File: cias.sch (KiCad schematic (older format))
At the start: 63 parts, among them CN13 KEYBOARD, CN6 SERIAL_DB25M, CN7 PARALLEL_DB25F, Q501 2N3904, Q502 2N3906, Q503 2N3906, Q711 2N3904, U38 MC1488, U39 MC1489, U42 NE555, U7 VIA_8520, U8 VIA_8520

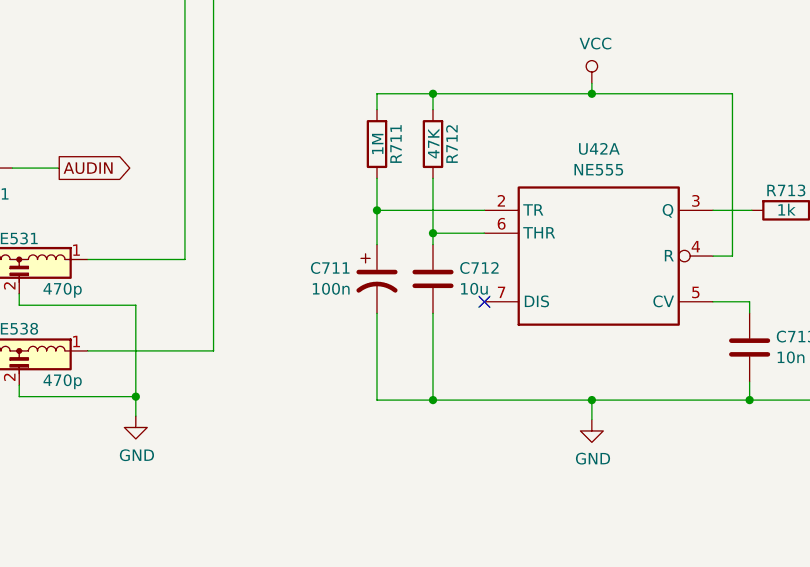
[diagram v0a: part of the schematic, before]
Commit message: Fix wrong symbols in schematics - Does not impact PCB
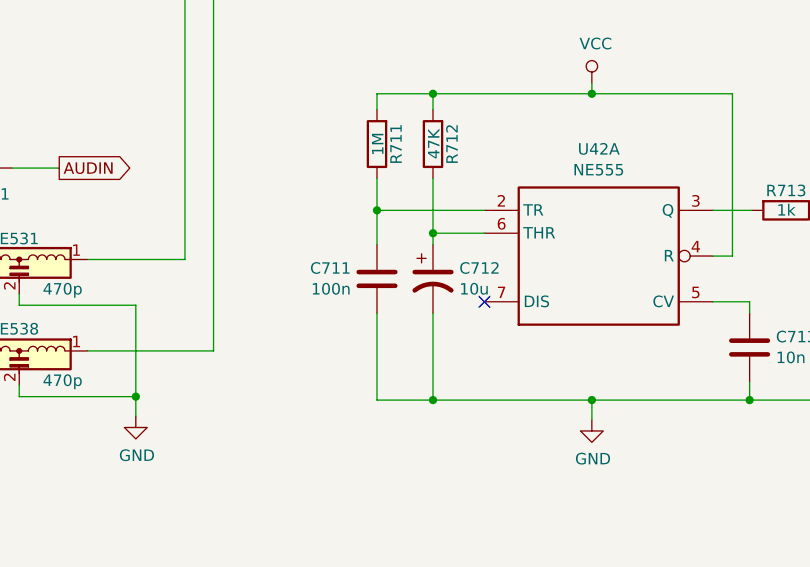
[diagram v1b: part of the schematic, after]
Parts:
- removed C711: 100n, Raemixx500:C_Axial_L9.0mm_D3.2mm_P12.70mm, symbol Device:CP1
- removed C712: 10u, Capacitor_THT:CP_Radial_D8.0mm_P5.00mm, symbol Device:C
- added C711: 100n, Raemixx500:C_Axial_L9.0mm_D3.2mm_P12.70mm, symbol Device:C
- added C712: 10u, Capacitor_THT:CP_Radial_D8.0mm_P5.00mm, symbol Device:CP1
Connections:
- net GND: now also C711.2, C712.2
- net at R711.1, U42.2 (TR): now also C711.1
- net at R712.1, U42.6 (THR): now also C712.1
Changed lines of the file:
@@
 Connection ~ 11990 7595
 NoConn ~ 12215 7895
-$Comp
-L Device:CP1 C711
-U 1 1 60129516
-P 11745 7795
-F 0 "C711" H 11631 7841 50  0000 R CNN
-F 1 "100n" H 11631 7750 50  0000 R CNN
-F 2 "Raemixx500:C_Axial_L9.0mm_D3.2mm_P12.70mm" H 11745 7795 50  0001 C CNN
-F 3 "~" H 11745 7795 50  0001 C CNN
-	1    11745 7795
-	1    0    0    -1
-$EndComp
-$Comp
-L Device:C C712
-U 1 1 60174D47
-P 11990 7795
-F 0 "C712" H 12105 7841 50  0000 L CNN
-F 1 "10u" H 12105 7750 50  0000 L CNN
-F 2 "Capacitor_THT:CP_Radial_D8.0mm_P5.00mm" H 12028 7645 50  0001 C CNN
-F 3 "~" H 11990 7795 50  0001 C CNN
-	1    11990 7795
-	1    0    0    -1
-$EndComp
 Wire Wire Line
 	11745 7645 11745 7495
@@
 	0    -1   -1   0
 $EndComp
+$Comp
+L Device:CP1 C712
+U 1 1 5EBE40E3
+P 11990 7795
+F 0 "C712" H 12105 7841 50  0000 L CNN
+F 1 "10u" H 12105 7750 50  0000 L CNN
+F 2 "Capacitor_THT:CP_Radial_D8.0mm_P5.00mm" H 11990 7795 50  0001 C CNN
+F 3 "~" H 11990 7795 50  0001 C CNN
+	1    11990 7795
+	1    0    0    -1
+$EndComp
+$Comp
+L Device:C C711
+U 1 1 5EBE45B6
+P 11745 7795
+F 0 "C711" H 11631 7841 50  0000 R CNN
+F 1 "100n" H 11631 7750 50  0000 R CNN
+F 2 "Raemixx500:C_Axial_L9.0mm_D3.2mm_P12.70mm" H 11783 7645 50  0001 C CNN
+F 3 "~" H 11745 7795 50  0001 C CNN
+	1    11745 7795
+	1    0    0    -1
+$EndComp
 Wire Bus Line

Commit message: Begin adding part numbers
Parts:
- C39, C7, C8: Cost (none) -> 0.071; MFG Name (none) -> KEMET; MFG Part Num (none) -> C410C103K1H5TAAUTO
- C42: Cost (none) -> 0.078; MFG Name (none) -> KEMET; MFG Part Num (none) -> C412C334M5U5TA; Optional (none) -> POR
- C501, C502: Cost (none) -> 0.078; MFG Name (none) -> KEMET; MFG Part Num (none) -> C412C334M5U5TA
- C711: Cost (none) -> 0.035; MFG Name (none) -> AVX; MFG Part Num (none) -> SA115C104KAR; Optional (none) -> POR
- C712, Q711, R711, R712, R713, U42: Optional (none) -> POR
- C713: Cost (none) -> 0.071; MFG Name (none) -> KEMET; MFG Part Num (none) -> C410C103K1H5TAAUTO; Optional (none) -> POR
- CN13: Optional (none) -> KEYBOARD
- CN6, U38, U39: Optional (none) -> SERIAL
- CN7: Optional (none) -> PARALLEL
- JP1, JP7B1: MFG Name (none) -> SKIP; MFG Part Num (none) -> SKIP; Optional (none) -> JMP
- R503, R504: Optional (none) -> ROM
- U7, U8: Optional (none) -> CUSTOM
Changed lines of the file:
@@
 F 2 "Package_DIP:DIP-40_W15.24mm_Socket_LongPads" H 3315 3460 50  0001 C CNN
 F 3 "DOCUMENTATION" H 3315 3460 50  0001 C CNN
+F 4 "CUSTOM" H 3315 3460 50  0001 C CNN "Optional"
 	1    3315 3460
 	1    0    0    -1
@@
 F 2 "Package_DIP:DIP-40_W15.24mm_Socket_LongPads" H 3315 6325 50  0001 C CNN
 F 3 "DOCUMENTATION" H 3315 6325 50  0001 C CNN
+F 4 "CUSTOM" H 3315 6325 50  0001 C CNN "Optional"
 	1    3315 6325
 	1    0    0    -1
@@
 F 2 "Raemixx500:DB_25F" H 9255 2590 50  0001 C CNN
 F 3 " ~" H 9255 2590 50  0001 C CNN
+F 4 "PARALLEL" H 9255 2590 50  0001 C CNN "Optional"
 	1    9255 2590
 	1    0    0    -1
@@
 F 2 "Raemixx500:DB_25M" H 9255 7610 50  0001 C CNN
 F 3 " ~" H 9255 7610 50  0001 C CNN
+F 4 "SERIAL" H 9255 7610 50  0001 C CNN "Optional"
 	1    9255 7610
 	1    0    0    1
@@
 F 2 "Raemixx500:C_Axial_L9.0mm_D3.2mm_P12.70mm" H 10050 7310 50  0001 C CNN
 F 3 "~" H 10050 7310 50  0001 C CNN
+F 4 "KEMET" H 10050 7310 50  0001 C CNN "MFG Name"
+F 5 "C412C334M5U5TA" H 10050 7310 50  0001 C CNN "MFG Part Num"
+F 6 "0.078" H 10050 7310 50  0001 C CNN "Cost"
 	1    10050 7310
 	0    1    1    0
@@
 F 2 "Raemixx500:C_Axial_L9.0mm_D3.2mm_P12.70mm" H 7935 8610 50  0001 C CNN
 F 3 "~" H 7935 8610 50  0001 C CNN
+F 4 "KEMET" H 7935 8610 50  0001 C CNN "MFG Name"
+F 5 "C412C334M5U5TA" H 7935 8610 50  0001 C CNN "MFG Part Num"
+F 6 "0.078" H 7935 8610 50  0001 C CNN "Cost"
 	1    7935 8610
 	0    1    1    0
@@
 F 2 "Package_DIP:DIP-14_W7.62mm_Socket_LongPads" H 7250 6360 50  0001 C CNN
 F 3 "DOCUMENTATION" H 7250 6260 50  0001 C CNN
+F 4 "SERIAL" H 7250 6610 50  0001 C CNN "Optional"
 	3    7250 6610
 	1    0    0    -1
@@
 F 2 "Package_DIP:DIP-14_W7.62mm_Socket_LongPads" H 7250 5945 50  0001 C CNN
 F 3 "DOCUMENTATION" H 7250 5845 50  0001 C CNN
+F 4 "SERIAL" H 7250 6195 50  0001 C CNN "Optional"
 	4    7250 6195
 	1    0    0    -1
@@
 F 2 "Package_DIP:DIP-14_W7.62mm_Socket_LongPads" H 7250 6760 50  0001 C CNN
 F 3 "DOCUMENTATION" H 7250 6660 50  0001 C CNN
+F 4 "SERIAL" H 7250 7010 50  0001 C CNN "Optional"
 	2    7250 7010
 	1    0    0    -1
@@
 F 2 "Package_DIP:DIP-14_W7.62mm_Socket_LongPads" H 6445 6560 50  0001 C CNN
 F 3 "DOCUMENTATION" H 6445 6460 50  0001 C CNN
+F 4 "SERIAL" H 6445 6810 50  0001 C CNN "Optional"
 	1    6445 6810
 	-1   0    0    -1
@@
 F 2 "Package_DIP:DIP-14_W7.62mm_Socket_LongPads" H 6090 7160 50  0001 C CNN
 F 3 "DOCUMENTATION" H 6090 7060 50  0001 C CNN
+F 4 "SERIAL" H 6090 7410 50  0001 C CNN "Optional"
 	2    6090 7410
 	-1   0    0    -1
@@
 F 2 "Package_DIP:DIP-14_W7.62mm_Socket_LongPads" H 5585 7560 50  0001 C CNN
 F 3 "DOCUMENTATION" H 5585 7460 50  0001 C CNN
+F 4 "SERIAL" H 5585 7810 50  0001 C CNN "Optional"
 	3    5585 7810
 	-1   0    0    -1
@@
 F 2 "Package_DIP:DIP-14_W7.62mm_Socket_LongPads" H 5585 6960 50  0001 C CNN
 F 3 "DOCUMENTATION" H 5585 6860 50  0001 C CNN
+F 4 "SERIAL" H 5585 7210 50  0001 C CNN "Optional"
 	4    5585 7210
 	-1   0    0    -1
@@
 F 2 "Package_DIP:DIP-14_W7.62mm_Socket_LongPads" H 1525 10110 50  0001 C CNN
 F 3 "DOCUMENTATION" H 1525 10010 50  0001 C CNN
+F 4 "SERIAL" H 1525 10360 50  0001 C CNN "Optional"
 	5    1525 10360
 	1    0    0    -1
@@
 F 2 "Package_DIP:DIP-14_W7.62mm_Socket_LongPads" H 2165 10110 50  0001 C CNN
 F 3 "DOCUMENTATION" H 2165 10010 50  0001 C CNN
+F 4 "SERIAL" H 2165 10360 50  0001 C CNN "Optional"
 	5    2165 10360
 	1    0    0    -1
@@
 F 2 "Raemixx500:C_Axial_L9.0mm_D3.2mm_P12.70mm" H 1228 10210 50  0001 C CNN
 F 3 "~" H 1190 10360 50  0001 C CNN
+F 4 "KEMET" H 1190 10360 50  0001 C CNN "MFG Name"
+F 5 "C410C103K1H5TAAUTO" H 1190 10360 50  0001 C CNN "MFG Part Num"
+F 6 "0.071" H 1190 10360 50  0001 C CNN "Cost"
 	1    1190 10360
 	1    0    0    -1
@@
 F 2 "Raemixx500:R_Axial_DIN0309_L9.0mm_D3.2mm_P12.70mm_Horizontal" V 12745 2745 50  0001 C CNN
 F 3 "~" H 12815 2745 50  0001 C CNN
+F 4 "ROM" H 12815 2745 50  0001 C CNN "Optional"
 	1    12815 2745
 	0    1    1    0
@@
 F 2 "Raemixx500:Keyboard_Connector" H 15110 3390 50  0001 C CNN
 F 3 "" H 15110 3390 50  0001 C CNN
+F 4 "KEYBOARD" H 15110 3390 50  0001 C CNN "Optional"
 	1    15110 3390
 	1    0    0    1
@@
 F 2 "Raemixx500:R_Axial_DIN0309_L9.0mm_D3.2mm_P12.70mm_Horizontal" V 12745 3675 50  0001 C CNN
 F 3 "~" H 12815 3675 50  0001 C CNN
+F 4 "ROM" H 12815 3675 50  0001 C CNN "Optional"
 	1    12815 3675
 	0    1    1    0
@@
 F 2 "Package_DIP:DIP-8_W7.62mm_Socket_LongPads" H 12715 7695 50  0001 C CNN
 F 3 "http://www.ti.com/lit/ds/symlink/ne555.pdf" H 12715 7695 50  0001 C CNN
+F 4 "POR" H 12715 7695 50  0001 C CNN "Optional"
 	1    12715 7695
 	1    0    0    -1
@@
 F 2 "Raemixx500:R_Axial_DIN0309_L9.0mm_D3.2mm_P12.70mm_Horizontal" V 11920 7205 50  0001 C CNN
 F 3 "~" H 11990 7205 50  0001 C CNN
+F 4 "POR" H 11990 7205 50  0001 C CNN "Optional"
 	1    11990 7205
 	-1   0    0    1
@@
 F 2 "Raemixx500:R_Axial_DIN0309_L9.0mm_D3.2mm_P12.70mm_Horizontal" V 11675 7205 50  0001 C CNN
 F 3 "~" H 11745 7205 50  0001 C CNN
+F 4 "POR" H 11745 7205 50  0001 C CNN "Optional"
 	1    11745 7205
 	-1   0    0    1
@@
 F 2 "Raemixx500:C_Axial_L9.0mm_D3.2mm_P12.70mm" H 13413 7945 50  0001 C CNN
 F 3 "~" H 13375 8095 50  0001 C CNN
+F 4 "KEMET" H 13375 8095 50  0001 C CNN "MFG Name"
+F 5 "C410C103K1H5TAAUTO" H 13375 8095 50  0001 C CNN "MFG Part Num"
+F 6 "0.071" H 13375 8095 50  0001 C CNN "Cost"
+F 7 "POR" H 13375 8095 50  0001 C CNN "Optional"
 	1    13375 8095
 	1    0    0    -1
@@
 F 2 "Package_TO_SOT_THT:TO-92L_Inline_Wide" H 14115 7420 50  0001 L CIN
 F 3 "https://www.fairchildsemi.com/datasheets/2N/2N3904.pdf" H 13915 7495 50  0001 L CNN
+F 4 "POR" H 13915 7495 50  0001 C CNN "Optional"
 	1    13915 7495
 	1    0    0    -1
@@
 F 2 "Raemixx500:Jumper2-Bridged" H 14310 7160 50  0001 C CNN
 F 3 "~" H 14310 7160 50  0001 C CNN
+F 4 "SKIP" H 14310 7160 50  0001 C CNN "MFG Name"
+F 5 "SKIP" H 14310 7160 50  0001 C CNN "MFG Part Num"
+F 6 "JMP" H 14310 7160 50  0001 C CNN "Optional"
 	1    14310 7160
 	1    0    0    -1
@@
 F 2 "Package_DIP:DIP-8_W7.62mm_Socket_LongPads" H 15630 7720 50  0001 C CNN
 F 3 "http://www.ti.com/lit/ds/symlink/lm555.pdf" H 15630 7720 50  0001 C CNN
+F 4 "POR" H 15630 7720 50  0001 C CNN "Optional"
 	2    15630 7720
 	1    0    0    -1
@@
 F 2 "Raemixx500:C_Axial_L6.3mm_D2.5mm_P10.16mm" H 15333 7635 50  0001 C CNN
 F 3 "~" H 15295 7785 50  0001 C CNN
+F 4 "KEMET" H 15295 7785 50  0001 C CNN "MFG Name"
+F 5 "C412C334M5U5TA" H 15295 7785 50  0001 C CNN "MFG Part Num"
+F 6 "0.078" H 15295 7785 50  0001 C CNN "Cost"
+F 7 "POR" H 15295 7785 50  0001 C CNN "Optional"
 	1    15295 7785
 	1    0    0    -1
@@
 F 2 "Package_DIP:DIP-40_W15.24mm_Socket_LongPads" H 6260 10260 50  0001 C CNN
 F 3 "DOCUMENTATION" H 6260 10260 50  0001 C CNN
+F 4 "CUSTOM" H 6260 10260 50  0001 C CNN "Optional"
 	2    6260 10260
 	1    0    0    -1
@@
 F 2 "Package_DIP:DIP-40_W15.24mm_Socket_LongPads" H 7675 10260 50  0001 C CNN
 F 3 "DOCUMENTATION" H 7675 10260 50  0001 C CNN
+F 4 "CUSTOM" H 7675 10260 50  0001 C CNN "Optional"
 	2    7675 10260
 	1    0    0    -1
@@
 F 2 "Raemixx500:C_Axial_L6.3mm_D2.5mm_P10.16mm" H 7043 10090 50  0001 C CNN
 F 3 "~" H 7005 10240 50  0001 C CNN
+F 4 "KEMET" H 7005 10240 50  0001 C CNN "MFG Name"
+F 5 "C410C103K1H5TAAUTO" H 7005 10240 50  0001 C CNN "MFG Part Num"
+F 6 "0.071" H 7005 10240 50  0001 C CNN "Cost"
 	1    7005 10240
 	1    0    0    -1
@@
 F 2 "Raemixx500:C_Axial_L6.3mm_D2.5mm_P10.16mm" H 8493 10090 50  0001 C CNN
 F 3 "~" H 8455 10240 50  0001 C CNN
+F 4 "KEMET" H 8455 10240 50  0001 C CNN "MFG Name"
+F 5 "C410C103K1H5TAAUTO" H 8455 10240 50  0001 C CNN "MFG Part Num"
+F 6 "0.071" H 8455 10240 50  0001 C CNN "Cost"
 	1    8455 10240
 	1    0    0    -1
@@
 F 2 "Raemixx500:R_Axial_DIN0309_L9.0mm_D3.2mm_P12.70mm_Horizontal" V 13465 7495 50  0001 C CNN
 F 3 "~" H 13535 7495 50  0001 C CNN
+F 4 "POR" H 13535 7495 50  0001 C CNN "Optional"
 	1    13535 7495
 	0    1    1    0
@@
 F 2 "Raemixx500:Jumper3-Bridged23" H 1240 4360 50  0001 C CNN
 F 3 "~" H 1240 4360 50  0001 C CNN
+F 4 "SKIP" H 1240 4360 50  0001 C CNN "MFG Name"
+F 5 "SKIP" H 1240 4360 50  0001 C CNN "MFG Part Num"
+F 6 "JMP" H 1240 4360 50  0001 C CNN "Optional"
 	1    1240 4360
 	0    -1   -1   0
@@
 F 2 "Capacitor_THT:CP_Radial_D8.0mm_P5.00mm" H 11990 7795 50  0001 C CNN
 F 3 "~" H 11990 7795 50  0001 C CNN
+F 4 "POR" H 11990 7795 50  0001 C CNN "Optional"
 	1    11990 7795
 	1    0    0    -1
@@
 F 2 "Raemixx500:C_Axial_L9.0mm_D3.2mm_P12.70mm" H 11783 7645 50  0001 C CNN
 F 3 "~" H 11745 7795 50  0001 C CNN
+F 4 "0.035" H 11745 7795 50  0001 C CNN "Cost"
+F 5 "AVX" H 11745 7795 50  0001 C CNN "MFG Name"
+F 6 "SA115C104KAR" H 11745 7795 50  0001 C CNN "MFG Part Num"
+F 7 "POR" H 11745 7795 50  0001 C CNN "Optional"
 	1    11745 7795
 	1    0    0    -1

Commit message: More part numbers
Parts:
- C501, C502, D501, E502, E503, E531, E532, E533, E534, E535, E536, E537, E538, Q501, R501, R502: Optional (none) -> SERIAL
- E501, E511, E512, E513, E514, E515, E516, E517, E518, E519, E520, E521, E522, E523, E524: Optional (none) -> PARALLEL
- E631, E632, Q502, Q503, R505, R506, R507: Optional (none) -> KEYBOARD
- R109: Optional (none) -> PARALLEL/SERIAL/FLOPPY
- R503, R504: Optional ROM -> KEYBOARD
- RP501: Optional (none) -> KEYBOARD/FLOPPY/PARALLEL/MEMORY

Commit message: More part numbers
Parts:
- C712: Cost (none) -> 0.196; MFG Name (none) -> PANASONIC; MFG Part Num (none) -> EEUFR1H100
- U38: Cost (none) -> 0.615; MFG Name (none) -> TI; MFG Part Num (none) -> MC1488N
- U39: Cost (none) -> 0.668; MFG Name (none) -> TI; MFG Part Num (none) -> MC1489N
- U42: Cost (none) -> 0.315; MFG Name (none) -> TI; MFG Part Num (none) -> NE555P
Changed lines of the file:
@@
 F 3 "DOCUMENTATION" H 7250 6260 50  0001 C CNN
 F 4 "SERIAL" H 7250 6610 50  0001 C CNN "Optional"
+F 5 "0.615" H 7250 6610 50  0001 C CNN "Cost"
+F 6 "TI" H 7250 6610 50  0001 C CNN "MFG Name"
+F 7 "MC1488N" H 7250 6610 50  0001 C CNN "MFG Part Num"
 	3    7250 6610
 	1    0    0    -1
@@
 F 3 "DOCUMENTATION" H 7250 5845 50  0001 C CNN
 F 4 "SERIAL" H 7250 6195 50  0001 C CNN "Optional"
+F 5 "0.615" H 7250 6195 50  0001 C CNN "Cost"
+F 6 "TI" H 7250 6195 50  0001 C CNN "MFG Name"
+F 7 "MC1488N" H 7250 6195 50  0001 C CNN "MFG Part Num"
 	4    7250 6195
 	1    0    0    -1
@@
 F 3 "DOCUMENTATION" H 7250 6660 50  0001 C CNN
 F 4 "SERIAL" H 7250 7010 50  0001 C CNN "Optional"
+F 5 "0.615" H 7250 7010 50  0001 C CNN "Cost"
+F 6 "TI" H 7250 7010 50  0001 C CNN "MFG Name"
+F 7 "MC1488N" H 7250 7010 50  0001 C CNN "MFG Part Num"
 	2    7250 7010
 	1    0    0    -1
@@
 F 3 "DOCUMENTATION" H 6445 6460 50  0001 C CNN
 F 4 "SERIAL" H 6445 6810 50  0001 C CNN "Optional"
+F 5 "0.668" H 6445 6810 50  0001 C CNN "Cost"
+F 6 "TI" H 6445 6810 50  0001 C CNN "MFG Name"
+F 7 "MC1489N" H 6445 6810 50  0001 C CNN "MFG Part Num"
 	1    6445 6810
 	-1   0    0    -1
@@
 F 3 "DOCUMENTATION" H 6090 7060 50  0001 C CNN
 F 4 "SERIAL" H 6090 7410 50  0001 C CNN "Optional"
+F 5 "0.668" H 6090 7410 50  0001 C CNN "Cost"
+F 6 "TI" H 6090 7410 50  0001 C CNN "MFG Name"
+F 7 "MC1489N" H 6090 7410 50  0001 C CNN "MFG Part Num"
 	2    6090 7410
 	-1   0    0    -1
@@
 F 3 "DOCUMENTATION" H 5585 7460 50  0001 C CNN
 F 4 "SERIAL" H 5585 7810 50  0001 C CNN "Optional"
+F 5 "0.668" H 5585 7810 50  0001 C CNN "Cost"
+F 6 "TI" H 5585 7810 50  0001 C CNN "MFG Name"
+F 7 "MC1489N" H 5585 7810 50  0001 C CNN "MFG Part Num"
 	3    5585 7810
 	-1   0    0    -1
@@
 F 3 "DOCUMENTATION" H 5585 6860 50  0001 C CNN
 F 4 "SERIAL" H 5585 7210 50  0001 C CNN "Optional"
+F 5 "0.668" H 5585 7210 50  0001 C CNN "Cost"
+F 6 "TI" H 5585 7210 50  0001 C CNN "MFG Name"
+F 7 "MC1489N" H 5585 7210 50  0001 C CNN "MFG Part Num"
 	4    5585 7210
 	-1   0    0    -1
@@
 F 3 "DOCUMENTATION" H 1525 10010 50  0001 C CNN
 F 4 "SERIAL" H 1525 10360 50  0001 C CNN "Optional"
+F 5 "0.668" H 1525 10360 50  0001 C CNN "Cost"
+F 6 "TI" H 1525 10360 50  0001 C CNN "MFG Name"
+F 7 "MC1489N" H 1525 10360 50  0001 C CNN "MFG Part Num"
 	5    1525 10360
 	1    0    0    -1
@@
 F 3 "DOCUMENTATION" H 2165 10010 50  0001 C CNN
 F 4 "SERIAL" H 2165 10360 50  0001 C CNN "Optional"
+F 5 "0.615" H 2165 10360 50  0001 C CNN "Cost"
+F 6 "TI" H 2165 10360 50  0001 C CNN "MFG Name"
+F 7 "MC1488N" H 2165 10360 50  0001 C CNN "MFG Part Num"
 	5    2165 10360
 	1    0    0    -1
@@
 F 3 "http://www.ti.com/lit/ds/symlink/ne555.pdf" H 12715 7695 50  0001 C CNN
 F 4 "POR" H 12715 7695 50  0001 C CNN "Optional"
+F 5 "0.315" H 12715 7695 50  0001 C CNN "Cost"
+F 6 "TI" H 12715 7695 50  0001 C CNN "MFG Name"
+F 7 "NE555P" H 12715 7695 50  0001 C CNN "MFG Part Num"
 	1    12715 7695
 	1    0    0    -1
@@
 F 3 "http://www.ti.com/lit/ds/symlink/lm555.pdf" H 15630 7720 50  0001 C CNN
 F 4 "POR" H 15630 7720 50  0001 C CNN "Optional"
+F 5 "0.315" H 15630 7720 50  0001 C CNN "Cost"
+F 6 "TI" H 15630 7720 50  0001 C CNN "MFG Name"
+F 7 "NE555P" H 15630 7720 50  0001 C CNN "MFG Part Num"
 	2    15630 7720
 	1    0    0    -1
@@
 F 3 "~" H 11990 7795 50  0001 C CNN
 F 4 "POR" H 11990 7795 50  0001 C CNN "Optional"
+F 5 "0.196" H 11990 7795 50  0001 C CNN "Cost"
+F 6 "PANASONIC" H 11990 7795 50  0001 C CNN "MFG Name"
+F 7 "EEUFR1H100" H 11990 7795 50  0001 C CNN "MFG Part Num"
 	1    11990 7795
 	1    0    0    -1
